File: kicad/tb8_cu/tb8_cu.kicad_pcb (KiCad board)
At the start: 4 copper layers, 210 x 85 mm, 45 parts, among them J1 Conn_02x25_Counter_Clockwise, U1 74AHCT74, U10 74AHCT193, U11 74AHCT193, U12 74AHCT193, U13 74AHCT193, U14 74AHCT573, U15 74AHCT573, U16 74HC00, U17 74HC00, U18 74HCT74, U19 74AHCT573, U2 74AHCT08, U20 74AHCT573, U21 74AHCT573, U22 74AHCT573, U3 74AHCT32, U4 74AHCT573, U5 74AHCT238, U6 74AHCT238, U7 74AHCT573, U8 74AHCT00, U9 74AHCT573

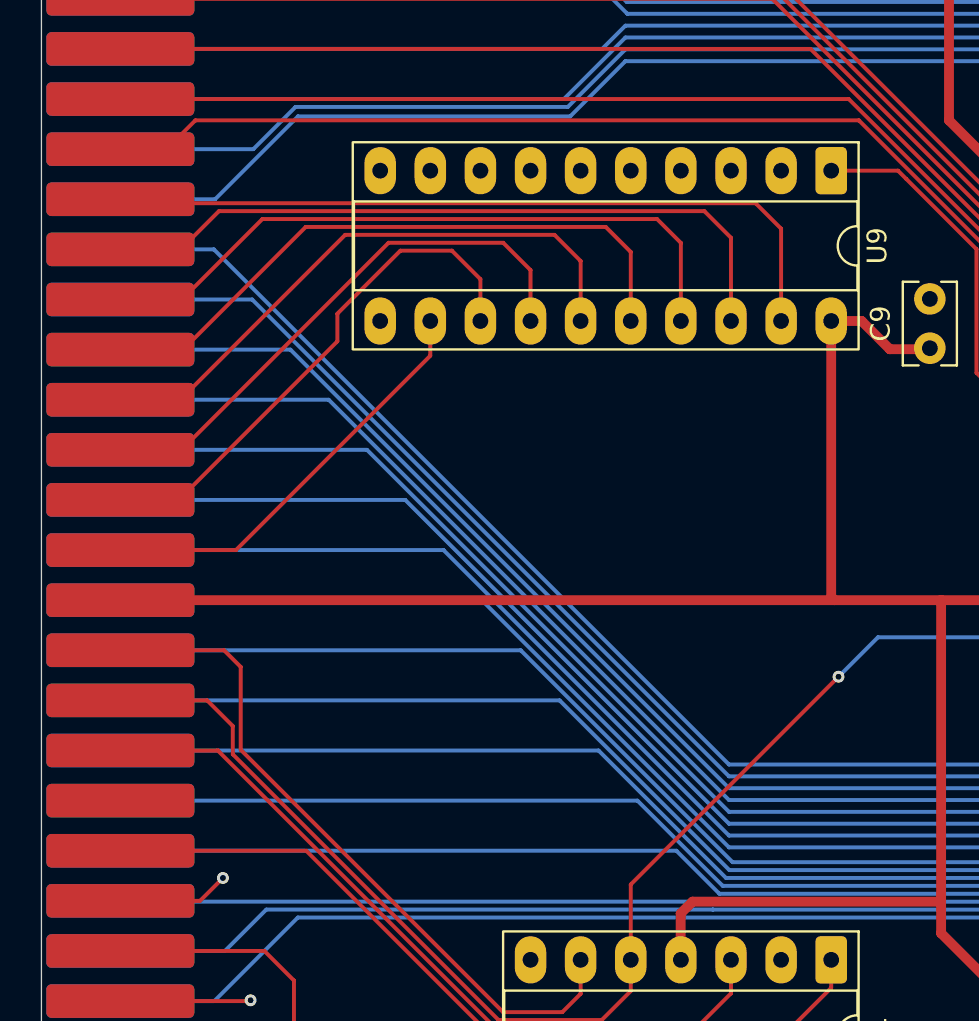
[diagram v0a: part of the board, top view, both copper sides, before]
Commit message: tb8_cu pcb routing cleanup
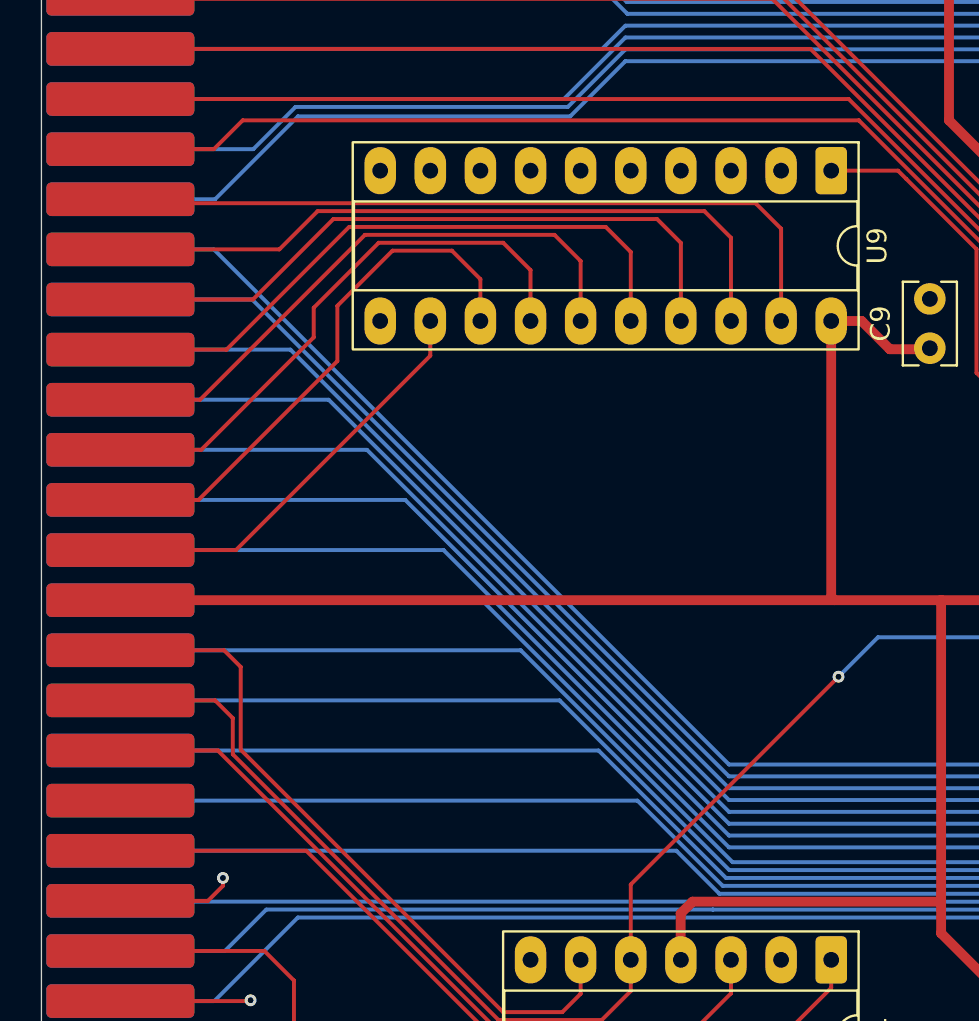
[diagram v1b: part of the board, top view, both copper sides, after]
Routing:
- net td5: track 321.3 -> 322.2 mm
- net td6: track 318.3 -> 319.1 mm
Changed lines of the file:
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@@
 	)
 	(segment
-		(start 28 89.54)
-		(end 31.06 89.54)
+		(start 36.06 89.54)
+		(end 37.999 87.601)
 		(width 0.2)
 		(layer "F.Cu")
@@
 	)
 	(segment
-		(start 32.999 87.601)
+		(start 37.999 87.601)
 		(end 57.601 87.601)
 		(width 0.2)
@@
 	)
 	(segment
-		(start 57.601 87.601)
-		(end 58.95 88.95)
+		(start 58.95 88.95)
+		(end 58.95 93.17)
 		(width 0.2)
 		(layer "F.Cu")
@@
 	)
 	(segment
-		(start 58.95 88.95)
-		(end 58.95 93.17)
+		(start 57.601 87.601)
+		(end 58.95 88.95)
 		(width 0.2)
 		(layer "F.Cu")
@@
 	)
 	(segment
-		(start 31.06 89.54)
-		(end 32.999 87.601)
+		(start 28 89.54)
+		(end 36.06 89.54)
 		(width 0.2)
 		(layer "F.Cu")
@@
 	)
 	(segment
-		(start 55.202 88.002)
-		(end 56.41 89.21)
+		(start 34.72 92.08)
+		(end 38.798 88.002)
 		(width 0.2)
 		(layer "F.Cu")
@@
 	)
 	(segment
-		(start 28 92.08)
-		(end 31.12 92.08)
+		(start 38.798 88.002)
+		(end 55.202 88.002)
 		(width 0.2)
 		(layer "F.Cu")
@@
 	)
 	(segment
-		(start 35.198 88.002)
-		(end 55.202 88.002)
+		(start 28 92.08)
+		(end 34.72 92.08)
 		(width 0.2)
 		(layer "F.Cu")
@@
 	)
 	(segment
-		(start 31.12 92.08)
-		(end 35.198 88.002)
+		(start 55.202 88.002)
+		(end 56.41 89.21)
 		(width 0.2)
 		(layer "F.Cu")
@@
 	)
 	(segment
-		(start 33.2 121.4)
-		(end 32.04 122.56)
+		(start 32.44 122.56)
+		(end 28 122.56)
 		(width 0.2)
 		(layer "F.Cu")
@@
 	)
 	(segment
-		(start 32.04 122.56)
-		(end 28 122.56)
+		(start 33.2 121.8)
+		(end 32.44 122.56)
+		(width 0.2)
+		(layer "F.Cu")
+		(net 15)
+	)
+	(segment
+		(start 33.2 121.4)
+		(end 33.2 121.8)
 		(width 0.2)
 		(layer "F.Cu")
@@
 	)
 	(segment
+		(start 48.79 90.59)
+		(end 48.79 93.17)
+		(width 0.2)
+		(layer "F.Cu")
+		(net 18)
+	)
+	(segment
 		(start 47.405 89.205)
 		(end 48.79 90.59)
@@
 	)
 	(segment
-		(start 31.1 99.7)
-		(end 41.595 89.205)
+		(start 37.8 94)
+		(end 37.8 92.5)
+		(width 0.2)
+		(layer "F.Cu")
+		(net 18)
+	)
+	(segment
+		(start 37.8 92.5)
+		(end 41.095 89.205)
 		(width 0.2)
 		(layer "F.Cu")
@@
 	)
 	(segment
-		(start 41.595 89.205)
+		(start 41.095 89.205)
 		(end 47.405 89.205)
 		(width 0.2)
@@
 	)
 	(segment
-		(start 48.79 90.59)
-		(end 48.79 93.17)
+		(start 32.1 99.7)
+		(end 37.8 94)
 		(width 0.2)
 		(layer "F.Cu")
@@
 	(segment
 		(start 28 99.7)
-		(end 31.1 99.7)
+		(end 32.1 99.7)
 		(width 0.2)
 		(layer "F.Cu")
@@
 	)
 	(segment
-		(start 44.806 89.606)
-		(end 46.25 91.05)
+		(start 39 95.2)
+		(end 39 92.4)
 		(width 0.2)
 		(layer "F.Cu")
@@
 	)
 	(segment
-		(start 30.96 102.24)
-		(end 39 94.2)
+		(start 44.806 89.606)
+		(end 46.25 91.05)
 		(width 0.2)
 		(layer "F.Cu")
@@
 	(segment
 		(start 28 102.24)
-		(end 30.96 102.24)
+		(end 31.96 102.24)
 		(width 0.2)
 		(layer "F.Cu")
@@
 	)
 	(segment
-		(start 39 92.8)
-		(end 42.194 89.606)
+		(start 41.794 89.606)
+		(end 44.806 89.606)
 		(width 0.2)
 		(layer "F.Cu")
@@
 	)
 	(segment
-		(start 42.194 89.606)
-		(end 44.806 89.606)
+		(start 46.25 91.05)
+		(end 46.25 93.17)
 		(width 0.2)
 		(layer "F.Cu")
@@
 	)
 	(segment
-		(start 46.25 91.05)
-		(end 46.25 93.17)
+		(start 31.96 102.24)
+		(end 39 95.2)
 		(width 0.2)
 		(layer "F.Cu")
@@
 	)
 	(segment
-		(start 39 94.2)
-		(end 39 92.8)
+		(start 39 92.4)
+		(end 41.794 89.606)
 		(width 0.2)
 		(layer "F.Cu")
@@
 	)
 	(segment
-		(start 31.04 97.16)
-		(end 39.396 88.804)
+		(start 40.396 88.804)
+		(end 50.004 88.804)
 		(width 0.2)
 		(layer "F.Cu")
@@
 	)
 	(segment
-		(start 50.004 88.804)
-		(end 51.33 90.13)
+		(start 32.04 97.16)
+		(end 40.396 88.804)
 		(width 0.2)
 		(layer "F.Cu")
@@
 	)
 	(segment
-		(start 28 97.16)
-		(end 31.04 97.16)
+		(start 50.004 88.804)
+		(end 51.33 90.13)
 		(width 0.2)
 		(layer "F.Cu")
@@
 	)
 	(segment
-		(start 39.396 88.804)
-		(end 50.004 88.804)
+		(start 28 97.16)
+		(end 32.04 97.16)
 		(width 0.2)
 		(layer "F.Cu")
@@
 	)
 	(segment
-		(start 30.34337 84.46)
-		(end 31.80337 83)
+		(start 28 84.46)
+		(end 32.74 84.46)
 		(width 0.2)
 		(layer "F.Cu")
@@
 	)
 	(segment
-		(start 31.80337 83)
-		(end 65.4329 83)
+		(start 71.796 89.3631)
+		(end 71.796 95.6315)
 		(width 0.2)
 		(layer "F.Cu")
@@
 	)
 	(segment
-		(start 75.5645 99.4)
-		(end 176.8 99.4)
+		(start 65.4329 83)
+		(end 71.796 89.3631)
 		(width 0.2)
 		(layer "F.Cu")
@@
 	)
 	(segment
-		(start 71.796 89.3631)
-		(end 71.796 95.6315)
+		(start 75.5645 99.4)
+		(end 176.8 99.4)
 		(width 0.2)
 		(layer "F.Cu")
@@
 	)
 	(segment
-		(start 65.4329 83)
-		(end 71.796 89.3631)
+		(start 71.796 95.6315)
+		(end 75.5645 99.4)
 		(width 0.2)
 		(layer "F.Cu")
@@
 	)
 	(segment
-		(start 28 84.46)
-		(end 30.34337 84.46)
+		(start 34.2 83)
+		(end 65.4329 83)
 		(width 0.2)
 		(layer "F.Cu")
@@
 	)
 	(segment
-		(start 71.796 95.6315)
-		(end 75.5645 99.4)
+		(start 32.74 84.46)
+		(end 34.2 83)
 		(width 0.2)
 		(layer "F.Cu")
@@
 	)
 	(segment
-		(start 183.87 64.07)
-		(end 183.87 65.55)
-		(width 0.2)
-		(layer "F.Cu")
-		(net 46)
-	)
-	(segment
 		(start 52.4 128.6)
 		(end 47.1671 128.6)
@@
 	)
 	(segment
-		(start 53.87 121.73)
-		(end 53.87 125.55)
+		(start 183.87 64.07)
+		(end 183.87 65.55)
 		(width 0.2)
 		(layer "F.Cu")
@@
 	)
 	(segment
-		(start 32.4 112.4)
-		(end 28 112.4)
+		(start 53.87 121.73)
+		(end 53.87 125.55)
 		(width 0.2)
 		(layer "F.Cu")
@@
 	)
 	(segment
-		(start 100.4 62.8)
-		(end 182.6 62.8)
+		(start 53.87 127.13)
+		(end 52.4 128.6)
 		(width 0.2)
 		(layer "F.Cu")
@@
 	(segment
 		(start 33.699 115.1319)
-		(end 33.699 113.699)
+		(end 33.699 113.299)
 		(width 0.2)
 		(layer "F.Cu")
@@
 	)
 	(segment
-		(start 53.87 127.13)
-		(end 52.4 128.6)
+		(start 47.1671 128.6)
+		(end 33.699 115.1319)
 		(width 0.2)
 		(layer "F.Cu")
@@
 	)
 	(segment
-		(start 64.4 111.2)
-		(end 53.87 121.73)
+		(start 100.4 62.8)
+		(end 182.6 62.8)
 		(width 0.2)
 		(layer "F.Cu")
@@
 	)
 	(segment
-		(start 33.699 113.699)
-		(end 32.4 112.4)
+		(start 33.699 113.299)
+		(end 32.8 112.4)
 		(width 0.2)
 		(layer "F.Cu")
@@
 	)
 	(segment
-		(start 47.1671 128.6)
-		(end 33.699 115.1319)
+		(start 64.4 111.2)
+		(end 53.87 121.73)
 		(width 0.2)
 		(layer "F.Cu")
@@
 	)
 	(segment
+		(start 32.8 112.4)
+		(end 28 112.4)
+		(width 0.2)
+		(layer "F.Cu")
+		(net 46)
+	)
+	(segment
 		(start 99.03 64.17)
 		(end 100.4 62.8)
@@
 	)
 	(segment
-		(start 28 94.62)
-		(end 31.18 94.62)
+		(start 53.87 89.67)
+		(end 53.87 93.17)
 		(width 0.2)
 		(layer "F.Cu")
@@
 	)
 	(segment
-		(start 31.18 94.62)
-		(end 37.397 88.403)
+		(start 33.38 94.62)
+		(end 39.597 88.403)
 		(width 0.2)
 		(layer "F.Cu")
@@
 	)
 	(segment
-		(start 53.87 89.67)
-		(end 53.87 93.17)
+		(start 28 94.62)
+		(end 33.38 94.62)
 		(width 0.2)
 		(layer "F.Cu")
@@
 	)
 	(segment
-		(start 37.397 88.403)
+		(start 39.597 88.403)
 		(end 52.603 88.403)
 		(width 0.2)

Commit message: Rename labels ste->stc and eql->cmp
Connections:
- net eql renamed cmp
- net ste_i renamed stc_i
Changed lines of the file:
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@@
 	(net 13 "td7")
 	(net 14 "a5")
-	(net 15 "eql")
+	(net 15 "cmp")
 	(net 16 "a15")
 	(net 17 "ta0")
@@
 	(net 55 "t_rdi")
 	(net 56 "ld_i")
-	(net 57 "ste_i")
+	(net 57 "stc_i")
 	(net 58 "ldi_i")
 	(net 59 "Net-(U2-Pad3)")
@@
 			(remove_unused_layers no)
 			(roundrect_rratio 0.15625)
-			(net 15 "eql")
+			(net 15 "cmp")
 			(pintype "input")
 		)
@@
 			(layers "*.Cu" "*.Mask")
 			(remove_unused_layers no)
-			(net 57 "ste_i")
+			(net 57 "stc_i")
 			(pintype "input")
 		)
@@
 			(layers "*.Cu" "*.Mask")
 			(remove_unused_layers no)
-			(net 57 "ste_i")
+			(net 57 "stc_i")
 			(pinfunction "Y3")
 			(pintype "output")
@@
 			(layers "F.Cu" "F.Mask")
 			(roundrect_rratio 0.15)
-			(net 15 "eql")
+			(net 15 "cmp")
 			(pinfunction "Pin_22")
 			(pintype "passive")

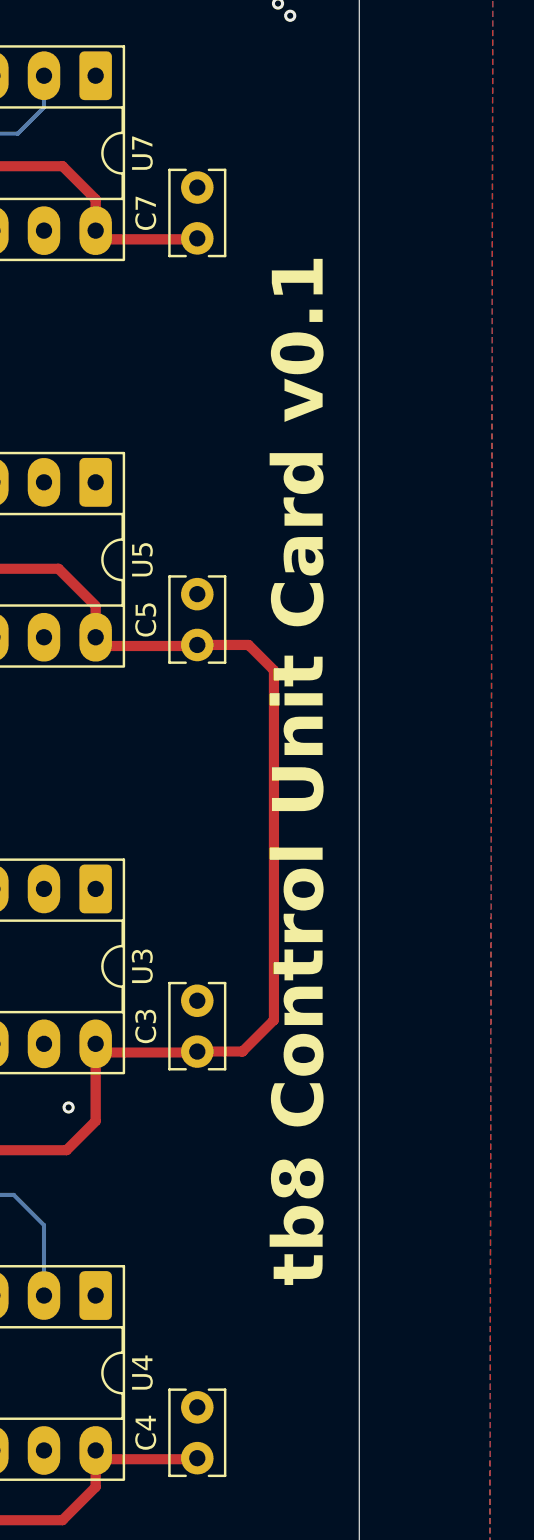
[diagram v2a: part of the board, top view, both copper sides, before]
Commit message: checked sch/pcb, pushes to v1.0, generated gerbers
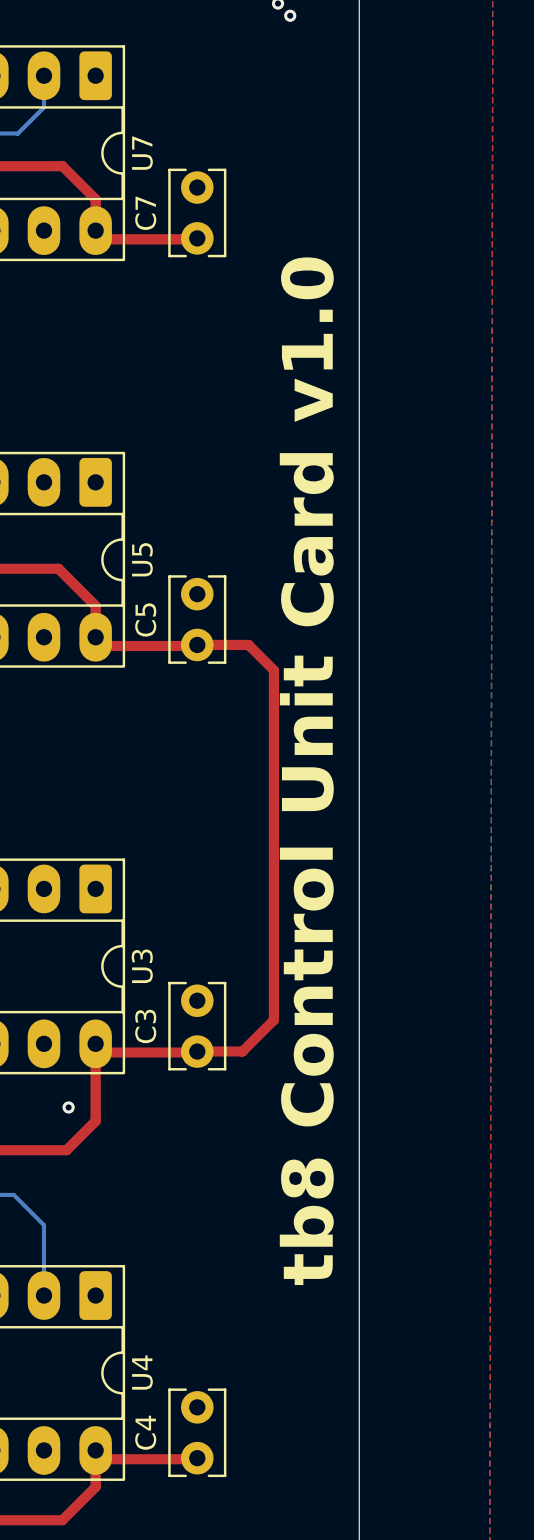
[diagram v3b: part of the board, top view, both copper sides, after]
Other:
- board text added: "tb8 Control Unit Card v1.0"
- board text removed: "tb8 Control Unit Card v0.1"
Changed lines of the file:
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@@
 	(title_block
 		(title "tb8 Control Unit Card")
-		(date "2025-11-29")
-		(rev "0.1")
+		(date "2025-12-13")
+		(rev "1.0")
 		(company "Dante Morelli")
 	)
@@
 			(outputformat 1)
 			(mirror no)
-			(drillshape 1)
+			(drillshape 0)
 			(scaleselection 1)
-			(outputdirectory "")
+			(outputdirectory "output/")
 		)
 	)
@@
 		(layer "Edge.Cuts")
 	)
-	(gr_text "tb8 Control Unit Card v0.1"
-		(at 240.5 99.7 90)
+	(gr_text "tb8 Control Unit Card v1.0"
+		(at 241 99.7 90)
 		(layer "F.SilkS")
 		(effects

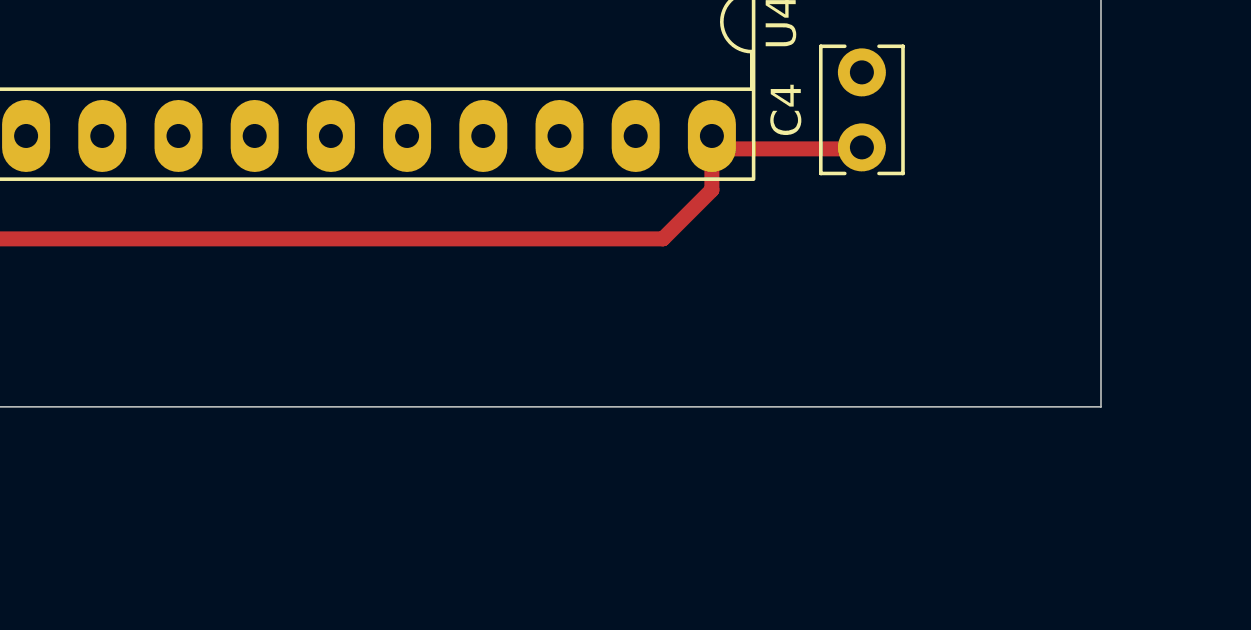
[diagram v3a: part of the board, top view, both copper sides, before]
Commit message: add name/date to silkscreen, gerber output to zip
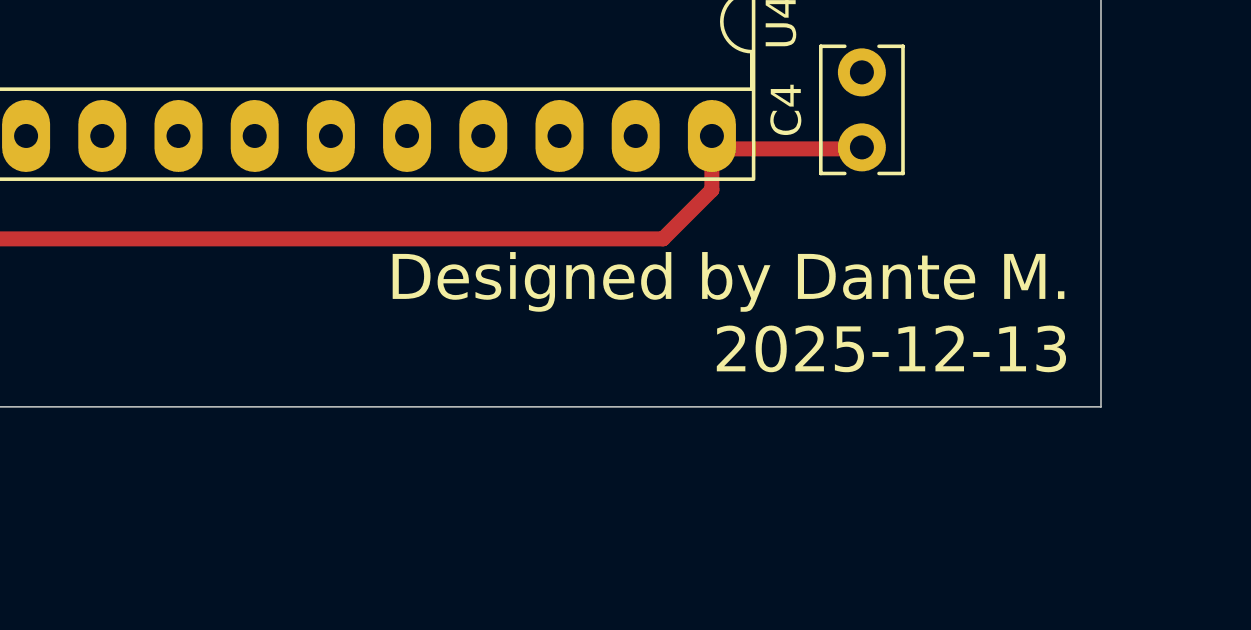
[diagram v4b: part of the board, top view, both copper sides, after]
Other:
- board text added: "Designed by Dante M. 2025-12-13"
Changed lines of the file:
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@@
+		)
+	)
+	(gr_text "Designed by Dante M.\n2025-12-13"
+		(at 241 141.2 0)
+		(layer "F.SilkS")
+		(effects
+			(font
+				(size 1.5 1.5)
+				(thickness 0.1875)
+			)
+			(justify right bottom)
 		)
 	)

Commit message: ground unused flipflop inputs
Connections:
- U1 pad 10: unconnected-(U1B-~{S}-Pad10) -> GND
- U1 pad 11: unconnected-(U1B-C-Pad11) -> GND
- U1 pad 12: unconnected-(U1B-D-Pad12) -> GND
- U1 pad 13: unconnected-(U1B-~{R}-Pad13) -> GND

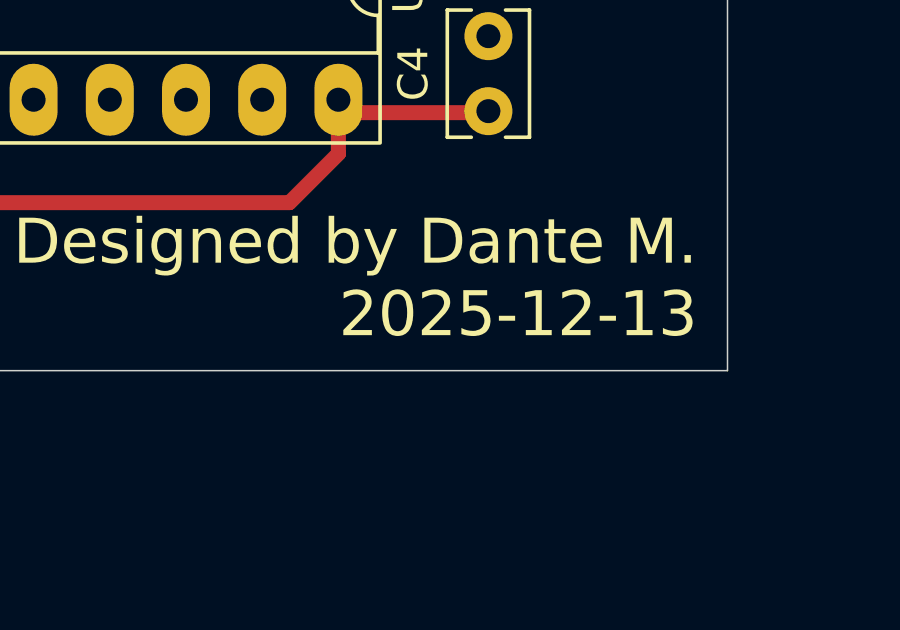
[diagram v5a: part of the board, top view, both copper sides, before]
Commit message: update sch pdf, update dates
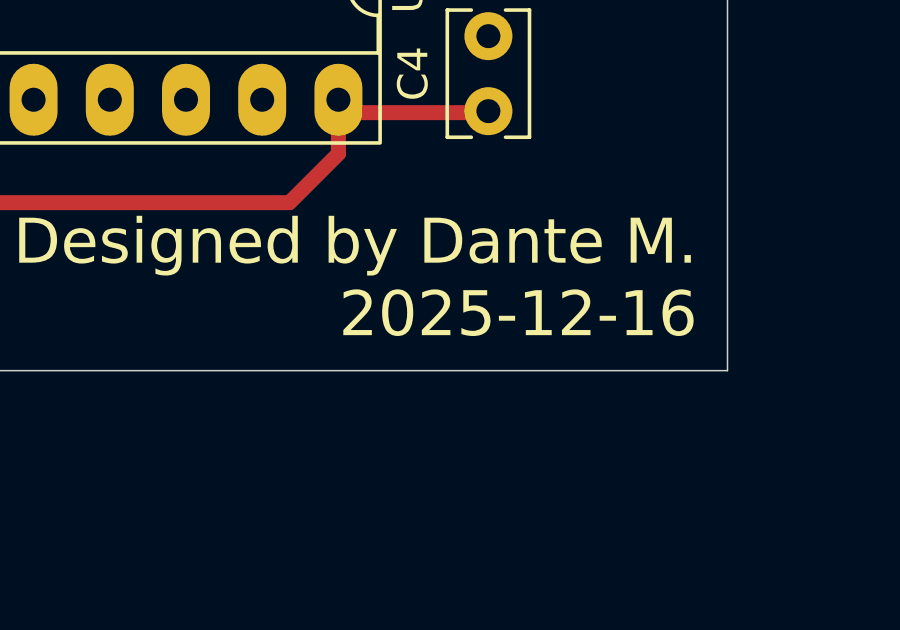
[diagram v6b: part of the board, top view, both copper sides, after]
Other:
- board text added: "Designed by Dante M. 2025-12-16"
- board text removed: "Designed by Dante M. 2025-12-13"
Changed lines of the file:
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@@
 	(title_block
 		(title "tb8 Control Unit Card")
-		(date "2025-12-13")
+		(date "2025-12-16")
 		(rev "1.0")
 		(company "Dante Morelli")
@@
 		)
 	)
-	(gr_text "Designed by Dante M.\n2025-12-13"
+	(gr_text "Designed by Dante M.\n2025-12-16"
 		(at 241 141.2 0)
 		(layer "F.SilkS")
